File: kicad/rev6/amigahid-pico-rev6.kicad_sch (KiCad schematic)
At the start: 115 parts, among them J1 A500 KBD OUT, J10 PS/2 KBD OUT, J11 DIN5 KBD IN, J12 PS/2 KBD IN, J13 USB-C AUX 5V, J2 DEBUG UART+SWD, J3 OLED I2C, J4 USB-A HOST, J7 SPARE GP28, J8 A500 KBD IN, J9 DIN5 KBD OUT, P1 DE9 MALE PORT 1, P2 DE9 MALE PORT 2, Q1 BSS138, Q10 BSS138, Q11 BSS138, Q12 BSS138, Q13 BSS138, Q14 BSS138, Q15 BSS138, Q16 BSS138, Q17 BSS138, Q18 BSS138, Q19 BSS138, Q2 BSS138, Q3 BSS138, Q4 BSS138, Q5 BSS138, Q6 BSS138, Q7 BSS138, Q8 BSS138, Q9 BSS138, U1 PicoW, U2 USBLC6-2SC6

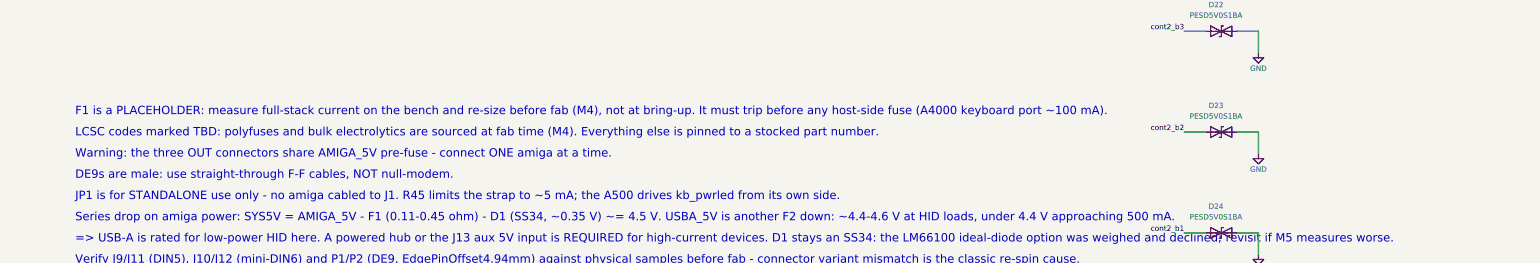
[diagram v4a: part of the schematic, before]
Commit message: kicad: void the module test-pad copper and tidy the rev6 board
the flat-mount build rests the pico w's bare underside test pads on the
carrier with nothing but solder resist between them, and rev6 was running
live copper under three of them: /cont1_v crossed tp6 (bootsel / qspi_ss),
/cont1_v_lo and /cont1_v crossed tp5, and ground pour filled tp4. tp6 held
low is an rp2040 that boots to mass storage for ever, and /cont1_v is a
5 v-side node pulled to sys5v, so that pad could also see overvoltage on a
3v3 pin. doc/errata.md already records the same class of fault on rev4.

so: both crossings move out, and an f.cu rule area at x 35.40-42.50,
y 47.76-49.76 keeps tracks, vias and pour out for good. /cont1_v_lo now
takes the 1.0 mm channel west of the band - q7 pad 2 straight down to the
existing b.cu node by r13 - which also drops 9 mm of copper and two vias
off that net. /cont1_v goes round the east side. the band covers tp4/tp5/
tp6 of a pico w or pico 2 w and tp5/tp6 of a plain pico; a plain pico's
tp4 is the one position with no room left, and errata says so.

also in this pass:

- 413 exactly duplicated track objects removed, plus four collinear
  slivers hiding inside longer segments of their own net (the 0.1 mm
  reverse stubs on /cont2_b1 and /cont2_b2 and a 0.071 mm +3v3 nub).
  style gate s3 goes green; s1 and s2 stay red, see below.
- the thirteen hand-soldered connectors and u1 get exclude_from_pos_files,
  so a regenerated cpl no longer offers jlc thirteen connectors and a
  51 mm module to place. jp1 already had it.
- u1's four usb shell pads lose their paste apertures. the footprint descr
  has claimed since it was written that reflow paste was deleted; the 40
  castellated pads were, these four were missed, and they sit directly
  under where the module has to lie flat.
- sixteen silkscreen strokes at 0.12 mm go to 0.15 mm, jlc's floor, and
  are pulled 0.02-0.03 mm off the board edge so widening them does not
  break the silk-to-edge rule. the u1 tap sl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
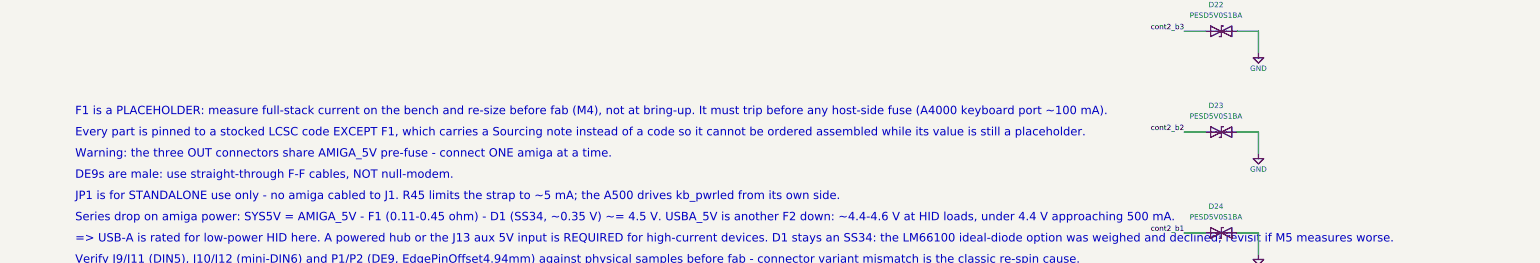
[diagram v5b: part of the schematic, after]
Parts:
- F1: LCSC C84140 -> (none); Sourcing (none) -> PLACEHOLDER - do not order assembled. Size F1 from a bench 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
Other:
- note added: "Every part is pinned to a stocked LCSC code EXCEPT F1, which carries a Sourcing note instead of a code so it cannot be ordered assembled while its value is still a placeholder."
- note removed: "LCSC codes marked TBD: polyfuses and bulk electrolytics are sourced at fab time (M4). Everything else is pinned to a stocked part number."
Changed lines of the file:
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@@
 			)
 		)
-		(property "LCSC" "C84140"
+		(property "Sourcing" "PLACEHOLDER - do not order assembled. Size F1 from a bench measurement of the full stack (plan predicts 350-500 mA), then hand-fit the 1812 part; MF-MSMF035/050/075 all share this land."
 			(at 314.96 264.16 0)
 			(hide yes)
@@
 		)
 	)
-	(text "LCSC codes marked TBD: polyfuses and bulk electrolytics are sourced at fab time (M4). Everything else is pinned to a stocked part number."
+	(text "Every part is pinned to a stocked LCSC code EXCEPT F1, which carries a Sourcing note instead of a code so it cannot be ordered assembled while its value is still a placeholder."
 		(exclude_from_sim no)
 		(at 459.74 377.19 0)

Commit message: kicad: rename the board to ux, drop the unsupported license line
silkscreen title is now "hid-pico Amiga UX", revision line "UX rev 1 - by
Jusii". the license assertion is removed: neither repo carries a license
file and both readmes point at epl-2.0 (tentative), so the board no longer
claims what no document supports. checker H2 re-targeted from the r6
marker to the UX product/revision marker in the same commit. the de9
footprint gains the verify-against-sample marker and the p1/p2 sourcing
fields get the corrected caliper dimensions (near pin row 7.78 mm, flange
holes 4.94 mm).
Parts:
- P1, P2: Sourcing Power Dynamics PDI-09S-5 (DE9 male, right-angle THT, 5.0 mm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 -> Power Dynamics PDI-09S-5 (DE9 male, right-angle THT, 5.34 m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
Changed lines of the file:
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@@
 			)
 		)
-		(property "Sourcing" "Power Dynamics PDI-09S-5 (DE9 male, right-angle THT, 5.0 mm footprint: near pin row 4.94 mm from the board edge, 2 x 3.2 mm holes on 25.0 mm centres; 7.2 mm / 0.318 in parts do NOT fit) - hand-solder, not JLC-assembled"
+		(property "Sourcing" "Power Dynamics PDI-09S-5 (DE9 male, right-angle THT, 5.34 mm footprint family: flange-screw holes 2 x 3.2 mm on 25.0 mm centres THROUGH the pcb at 4.94 mm from the board edge, near pin row 7.78 mm from the edge; 9.4 mm European-footprint and 7.2/8.08 mm parts do NOT fit) - hand-solder, not JLC-assembled"
 			(at 74.93 434.34 0)
 			(hide yes)
@@
 			)
 		)
-		(property "Sourcing" "Power Dynamics PDI-09S-5 (DE9 male, right-angle THT, 5.0 mm footprint: near pin row 4.94 mm from the board edge, 2 x 3.2 mm holes on 25.0 mm centres; 7.2 mm / 0.318 in parts do NOT fit) - hand-solder, not JLC-assembled"
-			(at 74.93 504.19 0)
-			(hide yes)
+		(property "Sourcing" "Power Dynamics PDI-09S-5 (DE9 male, right-angle THT, 5.34 mm footprint family: flange-screw holes 2 x 3.2 mm on 25.0 mm centres THROUGH the pcb at 4.94 mm from the board edge, near pin row 7.78 mm from the edge; 9.4 mm European-footprint and 7.2/8.08 mm parts do NOT fit) - hand-solder, not JLC-assembled"
+			(at 74.93 504.19 0)
+			(hide yes)

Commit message: kicad: retarget the de9 land to the .318in family
the rev6 DE9 land only ever matched Power Dynamics PDI-09S-5: a 5.34 mm
footprint with its boardlock holes collinear with the near pin row, which
is a PDI-proprietary trait, and the part is dead and unobtainable.  retarget
P1/P2 to the industry .318in/8.08 mm family, whose boardlock holes sit
midway between the pin rows.  primary buy is Kycon K22X-E9P-N; NorComp
182-009-113R531, TE 5747840-x, Wurth 618009231221 and Amphenol L717 code
33E are drop-in.

  * footprint renamed to the stock KiCad variant name
    EdgePinOffset7.70mm_Housed_MountingHolesOffset9.12mm, with its
    drawing taken from that variant: body, flange and boardlock legs all
    2.76 mm further from the pin rows.  the silk rails stop at local
    y=10.15 rather than the stock 10.48 so 0.15 mm silk clearance holds
    against the board edge.
  * pin coordinates unchanged - every D-sub family shares them - but the
    18 pin drills open 1.0 -> 1.1 mm for the 1.09 mm Kycon pin.  annulus
    stays 0.25 mm, well over the 0.13 mm floor.
  * the four boardlock pads move from local y=2.84 to y=1.42, i.e. from
    the near pin row to midway between the rows.  they stay 3.2 mm drill
    / 4.0 mm pad, plated, on GND with a solid zone connection.
  * south board edge moves 80.00 -> 82.76 so the near pin row sits the
    family's 7.70 mm behind it; the two south corner arcs and the side
    rails follow, and the south M3 holes keep their 4 mm corner inset at
    (4,78.76) and (96,78.76).  both GND pours extend to y=83.26.
  * re-routed around the moved boardlocks: /cont1_v and /cont1_b2_lo at
    P1 east, /cont2_v_lo, /cont2_vq and /cont2_hq at P2 west, /swclk at
    P2 east (which now hops to F.Cu to get past /cont2_b3).  no component
    moved.
  * the wider pin drills cost 0.05 mm of hole clearance, which the runs
    threading the two pin fields did not have; 30 runs slide 0.02-0.05 mm
    to re-centre in their corridors, and a 0.07 mm router spike on
    /co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
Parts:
- P1, P2: footprint rev6:DSUB-9_Pins_Horizontal_P2.77x2.84mm_EdgePinOffset4.94mm_Housed_MountingHolesOffset4.94mm -> rev6:DSUB-9_Pins_Horizontal_P2.77x2.84mm_EdgePinOffset7.70mm_Housed_MountingHolesOffset9.12mm; Sourcing Power Dynamics PDI-09S-5 (DE9 male, right-angle THT, 5.34 m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 -> Kycon K22X-E9P-N (DE9 male, right-angle THT, .318in/8.08mm 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
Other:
- note added: "Verify J9/J11 (DIN5), J10/J12 (mini-DIN6) and P1/P2 (DE9, EdgePinOffset7.70mm / MountingHolesOffset9.12mm) against physical samples before fab - connector variant mismatch is the classic re-spin cause."
- note removed: "Verify J9/J11 (DIN5), J10/J12 (mini-DIN6) and P1/P2 (DE9, EdgePinOffset4.94mm) against physical samples before fab - connector variant mismatch is the classic re-spin cause."
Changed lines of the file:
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@@
 			)
 		)
-		(property "Footprint" "rev6:DSUB-9_Pins_Horizontal_P2.77x2.84mm_EdgePinOffset4.94mm_Housed_MountingHolesOffset4.94mm"
+		(property "Footprint" "rev6:DSUB-9_Pins_Horizontal_P2.77x2.84mm_EdgePinOffset7.70mm_Housed_MountingHolesOffset9.12mm"
 			(at 74.93 434.34 0)
 			(hide yes)
@@
 			)
 		)
-		(property "Sourcing" "Power Dynamics PDI-09S-5 (DE9 male, right-angle THT, 5.34 mm footprint family: flange-screw holes 2 x 3.2 mm on 25.0 mm centres THROUGH the pcb at 4.94 mm from the board edge, near pin row 7.78 mm from the edge; 9.4 mm European-footprint and 7.2/8.08 mm parts do NOT fit) - hand-solder, not JLC-assembled"
+		(property "Sourcing" "Kycon K22X-E9P-N (DE9 male, right-angle THT, .318in/8.08mm footprint family: boardlock holes 2 x 3.2mm on 25.0mm centres MIDWAY between the pin rows, 1.42mm behind the near row; pin drills 1.1mm). Equivalents: NorComp 182-009-113R531, TE 5747840-x, Wurth 618009231221. The 5.34mm PDI family, 9.4mm European family and backset-alone matches do NOT fit - hole position vs the pin rows is the discriminator. - hand-solder, not JLC-assembled"
 			(at 74.93 434.34 0)
 			(hide yes)
@@
 			)
 		)
-		(property "Footprint" "rev6:DSUB-9_Pins_Horizontal_P2.77x2.84mm_EdgePinOffset4.94mm_Housed_MountingHolesOffset4.94mm"
+		(property "Footprint" "rev6:DSUB-9_Pins_Horizontal_P2.77x2.84mm_EdgePinOffset7.70mm_Housed_MountingHolesOffset9.12mm"
 			(at 74.93 504.19 0)
 			(hide yes)
@@
 			)
 		)
-		(property "Sourcing" "Power Dynamics PDI-09S-5 (DE9 male, right-angle THT, 5.34 mm footprint family: flange-screw holes 2 x 3.2 mm on 25.0 mm centres THROUGH the pcb at 4.94 mm from the board edge, near pin row 7.78 mm from the edge; 9.4 mm European-footprint and 7.2/8.08 mm parts do NOT fit) - hand-solder, not JLC-assembled"
+		(property "Sourcing" "Kycon K22X-E9P-N (DE9 male, right-angle THT, .318in/8.08mm footprint family: boardlock holes 2 x 3.2mm on 25.0mm centres MIDWAY between the pin rows, 1.42mm behind the near row; pin drills 1.1mm). Equivalents: NorComp 182-009-113R531, TE 5747840-x, Wurth 618009231221. The 5.34mm PDI family, 9.4mm European family and backset-alone matches do NOT fit - hole position vs the pin rows is the discriminator. - hand-solder, not JLC-assembled"
 			(at 74.93 504.19 0)
 			(hide yes)
@@
 		)
 	)
-	(text "Verify J9/J11 (DIN5), J10/J12 (mini-DIN6) and P1/P2 (DE9, EdgePinOffset4.94mm) against physical samples before fab - connector variant mismatch is the classic re-spin cause."
+	(text "Verify J9/J11 (DIN5), J10/J12 (mini-DIN6) and P1/P2 (DE9, EdgePinOffset7.70mm / MountingHolesOffset9.12mm) against physical samples before fab - connector variant mismatch is the classic re-spin cause."
 		(exclude_from_sim no)
 		(at 459.74 407.67 0)

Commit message: doc: swap out-of-stock mouser parts, fix the f1 low candidate to msmf030
msmf035 never existed in the bourns line - the 350 ma prediction in the
plan became a phantom part number; the real low candidate is msmf030
(300 ma hold). caps swapped to murata/kemet, ss34 to the diodes inc
b340a-13-f, the esd clamps to bourns cdsod323-t05c (nexperia ,135
packing as alternate), the cc resistors to panasonic erj-3ekf5101v.
cart csv customer part numbers now carry the AmigahidUX mark for
labeled bags.
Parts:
- F1: Sourcing PLACEHOLDER - do not order assembled. Size F1 from a bench measurement of the full stack (plan predicts 350-500 mA), then hand-fit the 1812 part; MF-MSMF035/050/075 all share this land. -> PLACEHOLDER - do not order assembled. Size F1 from a bench measurement of the full stack (plan predicts 350-500 mA), then hand-fit the 1812 part; MF-MSMF030/050/075 all share this land.
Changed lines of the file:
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@@
 			)
 		)
-		(property "Sourcing" "PLACEHOLDER - do not order assembled. Size F1 from a bench measurement of the full stack (plan predicts 350-500 mA), then hand-fit the 1812 part; MF-MSMF035/050/075 all share this land."
+		(property "Sourcing" "PLACEHOLDER - do not order assembled. Size F1 from a bench measurement of the full stack (plan predicts 350-500 mA), then hand-fit the 1812 part; MF-MSMF030/050/075 all share this land."
 			(at 314.96 264.16 0)
 			(hide yes)
